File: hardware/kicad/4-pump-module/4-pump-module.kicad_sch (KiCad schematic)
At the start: 30 parts, among them J1 Conn_02x03_Counter_Clockwise, J10 Pololu2-PWR, J3 PUMP 1, J4 PUMP 2, J5 PUMP 3, J6 PUMP 4, J7 Pololu1-CTRL, J8 Pololu1-PWR, J9 Pololu2-CTRL, U1 MCP23017x-x-SO

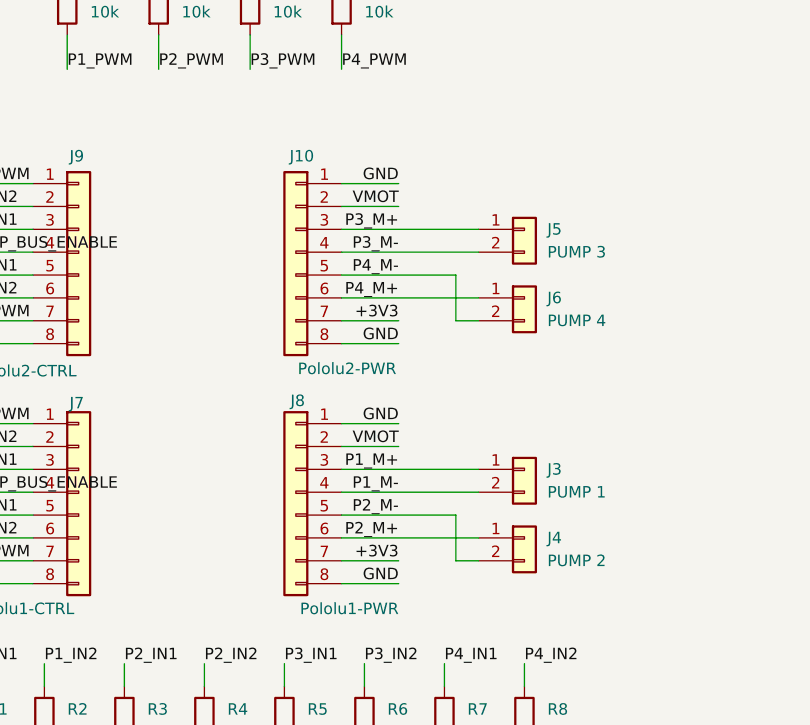
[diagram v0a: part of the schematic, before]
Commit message: Lock in both PCBs for fab and sync hardware, firmware pins, and procurement.
4-pump and main-controller KiCad layouts are ordered; motherboard GPIO map, CAD refs, bench logs, and AliExpress/OSH Park procurement notes are brought current so assembly can proceed when boards arrive.

Co-authored-by: Cursor <cursoragent@cursor.com>
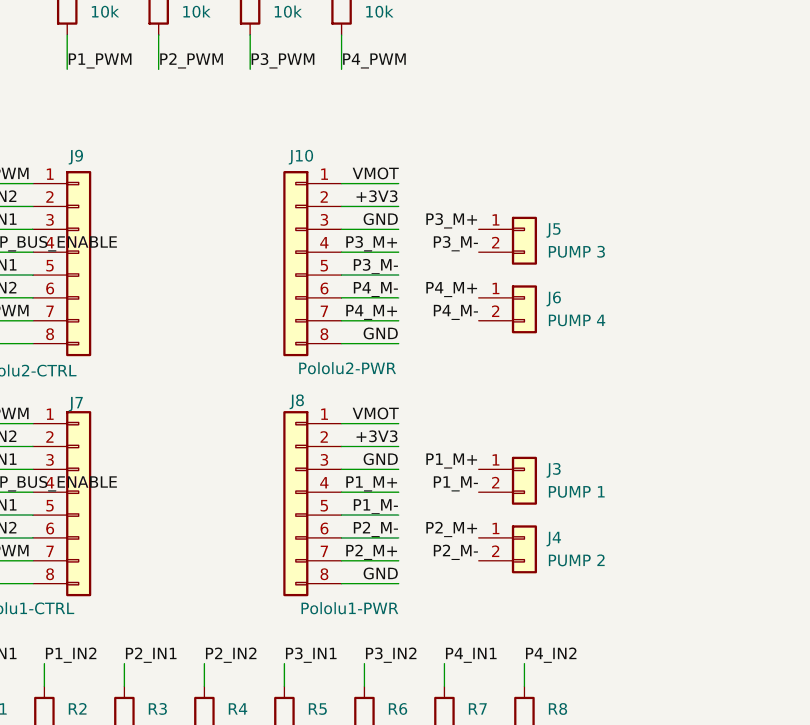
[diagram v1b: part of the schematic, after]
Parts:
- J1: footprint Connector_Molex:Molex_Micro-Fit_3.0_43045-0612_2x03_P3.00mm_Vertical -> Connector_Molex:Molex_Micro-Fit_3.0_43045-0600_2x03_P3.00mm_Horizontal
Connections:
- net +3V3: now also J10.2 (Pin_2), J8.2 (Pin_2); no longer J10.7 (Pin_7), J8.7 (Pin_7)
- net GND: now also J10.3 (Pin_3), J8.3 (Pin_3); no longer J10.1 (Pin_1), J8.1 (Pin_1)
- net P1_M+: now also J8.4 (Pin_4); no longer J8.3 (Pin_3)
- net P1_M-: now also J8.5 (Pin_5); no longer J8.4 (Pin_4)
- net P2_M+: now also J8.7 (Pin_7); no longer J8.6 (Pin_6)
- net P2_M-: now also J8.6 (Pin_6); no longer J8.5 (Pin_5)
- net P3_M+: now also J10.4 (Pin_4); no longer J10.3 (Pin_3)
- net P3_M-: now also J10.5 (Pin_5); no longer J10.4 (Pin_4)
- net P4_M+: now also J10.7 (Pin_7); no longer J10.6 (Pin_6)
- net P4_M-: now also J10.6 (Pin_6); no longer J10.5 (Pin_5)
- net VMOT: now also J10.1 (Pin_1), J8.1 (Pin_1); no longer J10.2 (Pin_2), J8.2 (Pin_2)
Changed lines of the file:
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@@
 	(wire
 		(pts
+			(xy 190.5 114.3) (xy 196.85 114.3)
+		)
+		(stroke
+			(width 0)
+			(type default)
+		)
+	)
+	(wire
+		(pts
 			(xy 86.36 116.84) (xy 83.82 116.84)
 		)
@@
 	(wire
 		(pts
-			(xy 180.34 50.8) (xy 190.5 50.8)
+			(xy 190.5 109.22) (xy 196.85 109.22)
 		)
 		(stroke
@@
 	(wire
 		(pts
-			(xy 123.19 83.82) (xy 127 83.82)
+			(xy 180.34 50.8) (xy 190.5 50.8)
 		)
 		(stroke
@@
 	(wire
 		(pts
-			(xy 137.16 25.4) (xy 128.27 25.4)
+			(xy 123.19 83.82) (xy 127 83.82)
 		)
 		(stroke
@@
 	(wire
 		(pts
-			(xy 170.18 50.8) (xy 175.26 50.8)
+			(xy 137.16 25.4) (xy 128.27 25.4)
 		)
 		(stroke
@@
 	(wire
 		(pts
-			(xy 90.17 114.3) (xy 97.79 114.3)
+			(xy 170.18 50.8) (xy 175.26 50.8)
 		)
 		(stroke
@@
 	(wire
 		(pts
-			(xy 92.71 78.74) (xy 97.79 78.74)
+			(xy 90.17 114.3) (xy 97.79 114.3)
 		)
 		(stroke
@@
 	(wire
 		(pts
-			(xy 190.5 111.76) (xy 203.2 111.76)
+			(xy 92.71 78.74) (xy 97.79 78.74)
 		)
 		(stroke
@@
 	(wire
 		(pts
-			(xy 73.66 116.84) (xy 73.66 114.3)
+			(xy 190.5 80.01) (xy 196.85 80.01)
 		)
 		(stroke
@@
 	(wire
 		(pts
-			(xy 148.59 87.63) (xy 156.21 87.63)
+			(xy 73.66 116.84) (xy 73.66 114.3)
 		)
 		(stroke
@@
 	(wire
 		(pts
-			(xy 157.48 128.27) (xy 157.48 130.81)
+			(xy 148.59 87.63) (xy 156.21 87.63)
 		)
 		(stroke
@@
 	(wire
 		(pts
-			(xy 148.59 128.27) (xy 148.59 130.81)
+			(xy 157.48 128.27) (xy 157.48 130.81)
 		)
 		(stroke
@@
 	(wire
 		(pts
-			(xy 92.71 81.28) (xy 97.79 81.28)
+			(xy 148.59 128.27) (xy 148.59 130.81)
 		)
 		(stroke
@@
 	(wire
 		(pts
-			(xy 148.59 82.55) (xy 156.21 82.55)
+			(xy 92.71 81.28) (xy 97.79 81.28)
 		)
 		(stroke
@@
 	(wire
 		(pts
-			(xy 190.5 92.71) (xy 196.85 92.71)
+			(xy 148.59 82.55) (xy 156.21 82.55)
 		)
 		(stroke
@@
 	(wire
 		(pts
-			(xy 190.5 87.63) (xy 205.74 87.63)
+			(xy 190.5 92.71) (xy 196.85 92.71)
 		)
 		(stroke
@@
 	(wire
 		(pts
-			(xy 205.74 90.17) (xy 203.2 90.17)
-		)
-		(stroke
-			(width 0)
-			(type default)
-		)
-	)
-	(wire
-		(pts
-			(xy 203.2 111.76) (xy 203.2 116.84)
-		)
-		(stroke
-			(width 0)
-			(type default)
-		)
-	)
-	(wire
-		(pts
 			(xy 90.17 123.19) (xy 90.17 114.3)
 		)
@@
 	(wire
 		(pts
-			(xy 190.5 109.22) (xy 205.74 109.22)
-		)
-		(stroke
-			(width 0)
-			(type default)
-		)
-	)
-	(wire
-		(pts
 			(xy 184.15 128.27) (xy 184.15 130.81)
 		)
@@
 	(wire
 		(pts
-			(xy 190.5 82.55) (xy 205.74 82.55)
+			(xy 190.5 82.55) (xy 196.85 82.55)
 		)
 		(stroke
@@
 	(wire
 		(pts
-			(xy 100.33 20.32) (xy 107.95 20.32)
+			(xy 190.5 106.68) (xy 196.85 106.68)
 		)
 		(stroke
@@
 	(wire
 		(pts
-			(xy 190.5 106.68) (xy 205.74 106.68)
+			(xy 100.33 20.32) (xy 107.95 20.32)
 		)
 		(stroke
@@
 	(wire
 		(pts
-			(xy 123.19 86.36) (xy 127 86.36)
+			(xy 190.5 87.63) (xy 196.85 87.63)
 		)
 		(stroke
@@
 	(wire
 		(pts
-			(xy 260.35 33.02) (xy 266.7 33.02)
+			(xy 123.19 86.36) (xy 127 86.36)
 		)
 		(stroke
@@
 	(wire
 		(pts
-			(xy 266.7 19.05) (xy 266.7 21.59)
+			(xy 260.35 33.02) (xy 266.7 33.02)
 		)
 		(stroke
@@
 	(wire
 		(pts
-			(xy 125.73 20.32) (xy 128.27 20.32)
+			(xy 266.7 19.05) (xy 266.7 21.59)
 		)
 		(stroke
@@
 	(wire
 		(pts
-			(xy 190.5 85.09) (xy 203.2 85.09)
+			(xy 125.73 20.32) (xy 128.27 20.32)
 		)
 		(stroke
@@
 	(wire
 		(pts
-			(xy 203.2 85.09) (xy 203.2 90.17)
-		)
-		(stroke
-			(width 0)
-			(type default)
-		)
-	)
-	(wire
-		(pts
 			(xy 148.59 116.84) (xy 156.21 116.84)
 		)
@@
 	(wire
 		(pts
-			(xy 205.74 116.84) (xy 203.2 116.84)
+			(xy 148.59 80.01) (xy 156.21 80.01)
 		)
 		(stroke
@@
 	(wire
 		(pts
-			(xy 148.59 80.01) (xy 156.21 80.01)
+			(xy 190.5 111.76) (xy 196.85 111.76)
 		)
 		(stroke
@@
 	(wire
 		(pts
-			(xy 190.5 114.3) (xy 205.74 114.3)
-		)
-		(stroke
-			(width 0)
-			(type default)
-		)
-	)
-	(wire
-		(pts
 			(xy 86.36 133.35) (xy 90.17 133.35)
 		)
@@
 	(wire
 		(pts
-			(xy 190.5 80.01) (xy 205.74 80.01)
+			(xy 175.26 138.43) (xy 180.34 138.43)
 		)
 		(stroke
@@
 	(wire
 		(pts
-			(xy 175.26 138.43) (xy 180.34 138.43)
+			(xy 190.5 101.6) (xy 196.85 101.6)
 		)
 		(stroke
@@
 	(wire
 		(pts
-			(xy 190.5 101.6) (xy 196.85 101.6)
+			(xy 227.33 19.05) (xy 227.33 21.59)
 		)
 		(stroke
@@
 	(wire
 		(pts
-			(xy 227.33 19.05) (xy 227.33 21.59)
+			(xy 190.5 85.09) (xy 196.85 85.09)
 		)
 		(stroke
@@
 		)
 	)
-	(label "P1_M+"
+	(label "GND"
 		(at 196.85 106.68 180)
 		(effects
@@
 		)
 	)
+	(label "P1_M+"
+		(at 205.74 106.68 180)
+		(effects
+			(font
+				(size 1.27 1.27)
+			)
+			(justify right bottom)
+		)
+	)
+	(label "P4_M+"
+		(at 205.74 87.63 180)
+		(effects
+			(font
+				(size 1.27 1.27)
+			)
+			(justify right bottom)
+		)
+	)
 	(label "GND"
 		(at 104.14 22.86 0)
@@
 		)
 	)
-	(label "P3_M-"
+	(label "P3_M+"
 		(at 196.85 82.55 180)
 		(effects
@@
 		)
 	)
-	(label "P2_M+"
+	(label "P3_M-"
+		(at 205.74 82.55 180)
+		(effects
+			(font
+				(size 1.27 1.27)
+			)
+			(justify right bottom)
+		)
+	)
+	(label "P2_M-"
 		(at 196.85 114.3 180)
 		(effects
@@
 		)
 	)
-	(label "VMOT"
+	(label "P4_M-"
+		(at 205.74 90.17 180)
+		(effects
+			(font
+				(size 1.27 1.27)
+			)
+			(justify right bottom)
+		)
+	)
+	(label "+3V3"
 		(at 196.85 104.14 180)
 		(effects
@@
 		)
 	)
+	(label "P3_M+"
+		(at 205.74 80.01 180)
+		(effects
+			(font
+				(size 1.27 1.27)
+			)
+			(justify right bottom)
+		)
+	)
 	(label "SDA"
 		(at 128.27 22.86 0)
@@
 		)
 	)
-	(label "+3V3"
+	(label "P4_M+"
 		(at 196.85 90.17 180)
 		(effects
@@
 		)
 	)
+	(label "P2_M+"
+		(at 205.74 114.3 180)
+		(effects
+			(font
+				(size 1.27 1.27)
+			)
+			(justify right bottom)
+		)
+	)
 	(label "P4_IN2"
 		(at 210.82 128.27 0)
@@
 		)
 	)
-	(label "GND"
+	(label "VMOT"
 		(at 196.85 74.93 180)
 		(effects
@@
 		)
 	)
-	(label "VMOT"
+	(label "+3V3"
 		(at 196.85 77.47 180)
 		(effects
@@
 		)
 	)
-	(label "GND"
+	(label "VMOT"
 		(at 196.85 101.6 180)
 		(effects
@@
 		)
 	)
-	(label "P1_M-"
+	(label "P1_M+"
 		(at 196.85 109.22 180)
 		(effects
@@
 		)
 	)
-	(label "+3V3"
+	(label "P2_M-"
+		(at 205.74 116.84 180)
+		(effects
+			(font
+				(size 1.27 1.27)
+			)
+			(justify right bottom)
+		)
+	)
+	(label "P2_M+"
 		(at 196.85 116.84 180)
 		(effects
@@
 		)
 	)
-	(label "P3_M+"
+	(label "GND"
 		(at 196.85 80.01 180)
 		(effects
@@
 		)
 	)
-	(label "P2_M-"
+	(label "P1_M-"
 		(at 196.85 111.76 180)
 		(effects
@@
 		)
 	)
-	(label "P4_M-"
+	(label "P3_M-"
 		(at 196.85 85.09 180)
 		(effects
@@
 		)
 	)
-	(label "P4_M+"
+	(label "P4_M-"
 		(at 196.85 87.63 180)
 		(effects
@@
 		)
 	)
+	(label "P1_M-"
+		(at 205.74 109.22 180)
+		(effects
+			(font
+				(size 1.27 1.27)
+			)
+			(justify right bottom)
+		)
+	)
 	(label "P1_IN1"
 		(at 148.59 106.68 0)
@@
 			)
 		)
-		(property "Footprint" "Connector_Molex:Molex_Micro-Fit_3.0_43045-0612_2x03_P3.00mm_Vertical"
+		(property "Footprint" "Connector_Molex:Molex_Micro-Fit_3.0_43045-0600_2x03_P3.00mm_Horizontal"
 			(at 118.11 22.86 0)
 			(hide yes)
